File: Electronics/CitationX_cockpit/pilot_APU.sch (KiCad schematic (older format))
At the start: 11 parts

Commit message: Electronics - Working on APUs
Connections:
- net DIO4: now also J?.10 (Pin_10)
- no-connect marks 9 -> 15
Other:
- moved on the sheet: J?
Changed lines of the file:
@@
 EELAYER 26 0
 EELAYER END
-$Descr A3 11693 16535 portrait
+$Descr A4 11693 8268
 encoding utf-8
 Sheet 6 10
@@
 L Connector:Screw_Terminal_01x10 J?
 U 1 1 5DC01A51
-P 7700 1750
+P 8000 1650
 AR Path="/5DB6029E/5DC01A51" Ref="J?"  Part="1"
 AR Path="/5DC174D6/5DC01A51" Ref="J?"  Part="1"
-F 0 "J?" H 7620 1117 50  0000 C CNN
-F 1 "Screw_Terminal_01x10" H 7620 1116 50  0001 C CNN
-F 2 "" H 7700 1750 50  0001 C CNN
-F 3 "~" H 7700 1750 50  0001 C CNN
-	1    7700 1750
-	-1   0    0    1
-$EndComp
-Text Label 7900 2150 0    50   ~ 0
+F 0 "J?" H 7920 1017 50  0000 C CNN
+F 1 "Screw_Terminal_01x10" H 7920 1016 50  0001 C CNN
+F 2 "" H 8000 1650 50  0001 C CNN
+F 3 "~" H 8000 1650 50  0001 C CNN
+	1    8000 1650
+	1    0    0    -1
+$EndComp
+Text Label 7800 1250 2    50   ~ 0
 CLK0
-Text Label 7900 2050 0    50   ~ 0
+Text Label 7800 1350 2    50   ~ 0
 DIO0
-Text Label 7900 1950 0    50   ~ 0
+Text Label 7800 1450 2    50   ~ 0
 CLK1
-Text Label 7900 1850 0    50   ~ 0
+Text Label 7800 1550 2    50   ~ 0
 DIO1
-Text Label 7900 1750 0    50   ~ 0
+Text Label 7800 1650 2    50   ~ 0
 CLK2
-Text Label 7900 1650 0    50   ~ 0
+Text Label 7800 1750 2    50   ~ 0
 DIO2
-Text Label 7900 1550 0    50   ~ 0
+Text Label 7800 1850 2    50   ~ 0
 CLK3
-Text Label 7900 1450 0    50   ~ 0
+Text Label 7800 1950 2    50   ~ 0
 DIO3
-Text Label 7900 1350 0    50   ~ 0
+Text Label 7800 2050 2    50   ~ 0
 CLK4
 $Comp
 L Connector:Screw_Terminal_01x10 J?
 U 1 1 5DC01A64
-P 8300 1750
+P 8700 1650
 AR Path="/5DB6029E/5DC01A64" Ref="J?"  Part="1"
 AR Path="/5DC174D6/5DC01A64" Ref="J?"  Part="1"
-F 0 "J?" H 8220 1117 50  0000 C CNN
-F 1 "Screw_Terminal_01x10" H 8220 1116 50  0001 C CNN
-F 2 "" H 8300 1750 50  0001 C CNN
-F 3 "~" H 8300 1750 50  0001 C CNN
-	1    8300 1750
-	-1   0    0    1
+F 0 "J?" H 8620 1017 50  0000 C CNN
+F 1 "Screw_Terminal_01x10" H 8620 1016 50  0001 C CNN
+F 2 "" H 8700 1650 50  0001 C CNN
+F 3 "~" H 8700 1650 50  0001 C CNN
+	1    8700 1650
+	1    0    0    -1
 $EndComp
 $Comp
 L power:+5V #PWR?
 U 1 1 5DC01A78
-P 8500 1550
+P 8500 1850
 AR Path="/5DB6029E/5DC01A78" Ref="#PWR?"  Part="1"
 AR Path="/5DC174D6/5DC01A78" Ref="#PWR?"  Part="1"
-F 0 "#PWR?" H 8500 1400 50  0001 C CNN
-F 1 "+5V" V 8515 1678 50  0000 L CNN
+F 0 "#PWR?" H 8500 1700 50  0001 C CNN
+F 1 "+5V" V 8515 1978 50  0000 L CNN
+F 2 "" H 8500 1850 50  0001 C CNN
+F 3 "" H 8500 1850 50  0001 C CNN
+	1    8500 1850
+	0    -1   -1   0
+$EndComp
+$Comp
+L power:+5V #PWR?
+U 1 1 5DC01A7E
+P 8500 1950
+AR Path="/5DB6029E/5DC01A7E" Ref="#PWR?"  Part="1"
+AR Path="/5DC174D6/5DC01A7E" Ref="#PWR?"  Part="1"
+F 0 "#PWR?" H 8500 1800 50  0001 C CNN
+F 1 "+5V" V 8515 2078 50  0000 L CNN
+F 2 "" H 8500 1950 50  0001 C CNN
+F 3 "" H 8500 1950 50  0001 C CNN
+	1    8500 1950
+	0    -1   -1   0
+$EndComp
+$Comp
+L power:+5V #PWR?
+U 1 1 5DC01A84
+P 8500 2050
+AR Path="/5DB6029E/5DC01A84" Ref="#PWR?"  Part="1"
+AR Path="/5DC174D6/5DC01A84" Ref="#PWR?"  Part="1"
+F 0 "#PWR?" H 8500 1900 50  0001 C CNN
+F 1 "+5V" V 8515 2178 50  0000 L CNN
+F 2 "" H 8500 2050 50  0001 C CNN
+F 3 "" H 8500 2050 50  0001 C CNN
+	1    8500 2050
+	0    -1   -1   0
+$EndComp
+$Comp
+L power:+5V #PWR?
+U 1 1 5DC01A8A
+P 8500 2150
+AR Path="/5DB6029E/5DC01A8A" Ref="#PWR?"  Part="1"
+AR Path="/5DC174D6/5DC01A8A" Ref="#PWR?"  Part="1"
+F 0 "#PWR?" H 8500 2000 50  0001 C CNN
+F 1 "+5V" V 8515 2278 50  0000 L CNN
+F 2 "" H 8500 2150 50  0001 C CNN
+F 3 "" H 8500 2150 50  0001 C CNN
+	1    8500 2150
+	0    -1   -1   0
+$EndComp
+$Comp
+L power:GND #PWR?
+U 1 1 5DC01AA2
+P 8500 1250
+AR Path="/5DB6029E/5DC01AA2" Ref="#PWR?"  Part="1"
+AR Path="/5DC174D6/5DC01AA2" Ref="#PWR?"  Part="1"
+F 0 "#PWR?" H 8500 1000 50  0001 C CNN
+F 1 "GND" H 8505 1077 50  0000 C CNN
+F 2 "" H 8500 1250 50  0001 C CNN
+F 3 "" H 8500 1250 50  0001 C CNN
+	1    8500 1250
+	0    1    1    0
+$EndComp
+$Comp
+L power:GND #PWR?
+U 1 1 5DC01AA8
+P 8500 1350
+AR Path="/5DB6029E/5DC01AA8" Ref="#PWR?"  Part="1"
+AR Path="/5DC174D6/5DC01AA8" Ref="#PWR?"  Part="1"
+F 0 "#PWR?" H 8500 1100 50  0001 C CNN
+F 1 "GND" H 8505 1177 50  0000 C CNN
+F 2 "" H 8500 1350 50  0001 C CNN
+F 3 "" H 8500 1350 50  0001 C CNN
+	1    8500 1350
+	0    1    1    0
+$EndComp
+$Comp
+L power:GND #PWR?
+U 1 1 5DC01AAE
+P 8500 1450
+AR Path="/5DB6029E/5DC01AAE" Ref="#PWR?"  Part="1"
+AR Path="/5DC174D6/5DC01AAE" Ref="#PWR?"  Part="1"
+F 0 "#PWR?" H 8500 1200 50  0001 C CNN
+F 1 "GND" H 8505 1277 50  0000 C CNN
+F 2 "" H 8500 1450 50  0001 C CNN
+F 3 "" H 8500 1450 50  0001 C CNN
+	1    8500 1450
+	0    1    1    0
+$EndComp
+$Comp
+L power:GND #PWR?
+U 1 1 5DC01AB4
+P 8500 1550
+AR Path="/5DB6029E/5DC01AB4" Ref="#PWR?"  Part="1"
+AR Path="/5DC174D6/5DC01AB4" Ref="#PWR?"  Part="1"
+F 0 "#PWR?" H 8500 1300 50  0001 C CNN
+F 1 "GND" H 8505 1377 50  0000 C CNN
 F 2 "" H 8500 1550 50  0001 C CNN
 F 3 "" H 8500 1550 50  0001 C CNN
@@
 $EndComp
 $Comp
-L power:+5V #PWR?
-U 1 1 5DC01A7E
-P 8500 1450
-AR Path="/5DB6029E/5DC01A7E" Ref="#PWR?"  Part="1"
-AR Path="/5DC174D6/5DC01A7E" Ref="#PWR?"  Part="1"
-F 0 "#PWR?" H 8500 1300 50  0001 C CNN
-F 1 "+5V" V 8515 1578 50  0000 L CNN
-F 2 "" H 8500 1450 50  0001 C CNN
-F 3 "" H 8500 1450 50  0001 C CNN
-	1    8500 1450
-	0    1    1    0
-$EndComp
-$Comp
-L power:+5V #PWR?
-U 1 1 5DC01A84
-P 8500 1350
-AR Path="/5DB6029E/5DC01A84" Ref="#PWR?"  Part="1"
-AR Path="/5DC174D6/5DC01A84" Ref="#PWR?"  Part="1"
-F 0 "#PWR?" H 8500 1200 50  0001 C CNN
-F 1 "+5V" V 8515 1478 50  0000 L CNN
-F 2 "" H 8500 1350 50  0001 C CNN
-F 3 "" H 8500 1350 50  0001 C CNN
-	1    8500 1350
-	0    1    1    0
-$EndComp
-$Comp
-L power:+5V #PWR?
-U 1 1 5DC01A8A
-P 8500 1250
-AR Path="/5DB6029E/5DC01A8A" Ref="#PWR?"  Part="1"
-AR Path="/5DC174D6/5DC01A8A" Ref="#PWR?"  Part="1"
-F 0 "#PWR?" H 8500 1100 50  0001 C CNN
-F 1 "+5V" V 8515 1378 50  0000 L CNN
-F 2 "" H 8500 1250 50  0001 C CNN
-F 3 "" H 8500 1250 50  0001 C CNN
-	1    8500 1250
-	0    1    1    0
-$EndComp
-$Comp
-L power:GND #PWR?
-U 1 1 5DC01AA2
-P 8500 2150
-AR Path="/5DB6029E/5DC01AA2" Ref="#PWR?"  Part="1"
-AR Path="/5DC174D6/5DC01AA2" Ref="#PWR?"  Part="1"
-F 0 "#PWR?" H 8500 1900 50  0001 C CNN
-F 1 "GND" H 8505 1977 50  0000 C CNN
-F 2 "" H 8500 2150 50  0001 C CNN
-F 3 "" H 8500 2150 50  0001 C CNN
-	1    8500 2150
-	0    -1   -1   0
-$EndComp
-$Comp
-L power:GND #PWR?
-U 1 1 5DC01AA8
-P 8500 2050
-AR Path="/5DB6029E/5DC01AA8" Ref="#PWR?"  Part="1"
-AR Path="/5DC174D6/5DC01AA8" Ref="#PWR?"  Part="1"
-F 0 "#PWR?" H 8500 1800 50  0001 C CNN
-F 1 "GND" H 8505 1877 50  0000 C CNN
-F 2 "" H 8500 2050 50  0001 C CNN
-F 3 "" H 8500 2050 50  0001 C CNN
-	1    8500 2050
-	0    -1   -1   0
-$EndComp
-$Comp
-L power:GND #PWR?
-U 1 1 5DC01AAE
-P 8500 1950
-AR Path="/5DB6029E/5DC01AAE" Ref="#PWR?"  Part="1"
-AR Path="/5DC174D6/5DC01AAE" Ref="#PWR?"  Part="1"
-F 0 "#PWR?" H 8500 1700 50  0001 C CNN
-F 1 "GND" H 8505 1777 50  0000 C CNN
-F 2 "" H 8500 1950 50  0001 C CNN
-F 3 "" H 8500 1950 50  0001 C CNN
-	1    8500 1950
-	0    -1   -1   0
-$EndComp
-$Comp
-L power:GND #PWR?
-U 1 1 5DC01AB4
-P 8500 1850
-AR Path="/5DB6029E/5DC01AB4" Ref="#PWR?"  Part="1"
-AR Path="/5DC174D6/5DC01AB4" Ref="#PWR?"  Part="1"
-F 0 "#PWR?" H 8500 1600 50  0001 C CNN
-F 1 "GND" H 8505 1677 50  0000 C CNN
-F 2 "" H 8500 1850 50  0001 C CNN
-F 3 "" H 8500 1850 50  0001 C CNN
-	1    8500 1850
-	0    -1   -1   0
-$EndComp
-$Comp
 L power:GND #PWR?
 U 1 1 5DC01ABA
-P 8500 1750
+P 8500 1650
 AR Path="/5DB6029E/5DC01ABA" Ref="#PWR?"  Part="1"
 AR Path="/5DC174D6/5DC01ABA" Ref="#PWR?"  Part="1"
-F 0 "#PWR?" H 8500 1500 50  0001 C CNN
-F 1 "GND" H 8505 1577 50  0000 C CNN
-F 2 "" H 8500 1750 50  0001 C CNN
-F 3 "" H 8500 1750 50  0001 C CNN
-	1    8500 1750
-	0    -1   -1   0
+F 0 "#PWR?" H 8500 1400 50  0001 C CNN
+F 1 "GND" H 8505 1477 50  0000 C CNN
+F 2 "" H 8500 1650 50  0001 C CNN
+F 3 "" H 8500 1650 50  0001 C CNN
+	1    8500 1650
+	0    1    1    0
 $EndComp
 Wire Notes Line
@@
 L power:+5V #PWR?
 U 1 1 5DC01BE0
-P 8450 1650
+P 8550 1750
 AR Path="/5DB6029E/5DC01BE0" Ref="#PWR?"  Part="1"
 AR Path="/5DC174D6/5DC01BE0" Ref="#PWR?"  Part="1"
-F 0 "#PWR?" H 8450 1500 50  0001 C CNN
-F 1 "+5V" V 8465 1778 50  0000 L CNN
-F 2 "" H 8450 1650 50  0001 C CNN
-F 3 "" H 8450 1650 50  0001 C CNN
-	1    8450 1650
-	0    1    1    0
+F 0 "#PWR?" H 8550 1600 50  0001 C CNN
+F 1 "+5V" V 8565 1878 50  0000 L CNN
+F 2 "" H 8550 1750 50  0001 C CNN
+F 3 "" H 8550 1750 50  0001 C CNN
+	1    8550 1750
+	0    -1   -1   0
 $EndComp
 $Comp
@@
 Wire Wire Line
 	4750 3950 5450 3950
+Text Label 7800 2150 2    50   ~ 0
+DIO4
+NoConn ~ 6600 1850
+NoConn ~ 6600 1950
+NoConn ~ 6600 2050
+NoConn ~ 5100 1850
+NoConn ~ 5100 1950
+NoConn ~ 5100 2050
 $EndSCHEMATC

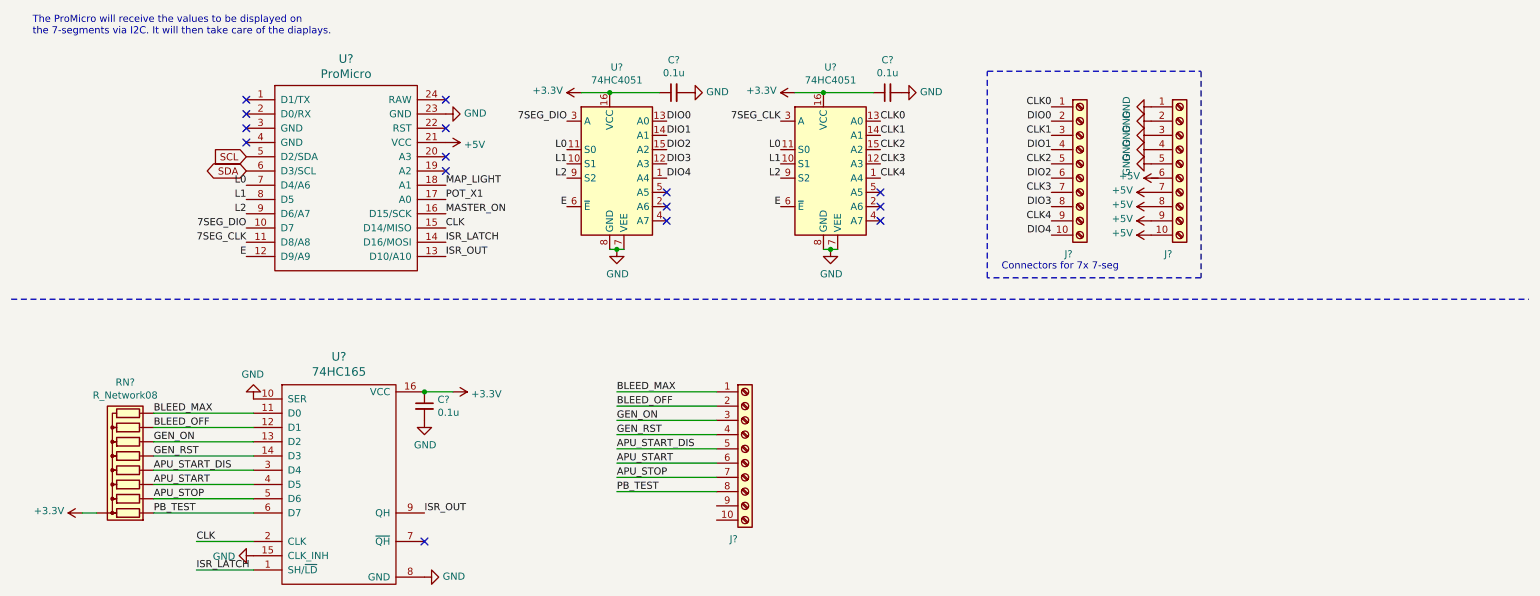
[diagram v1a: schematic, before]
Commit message: Electronics - Misc. works
Continued (and checked board). All connections are probably OK.
Fixed hierarchical pins in APUs (affects all schematics)
Numbered elements for testing schematics
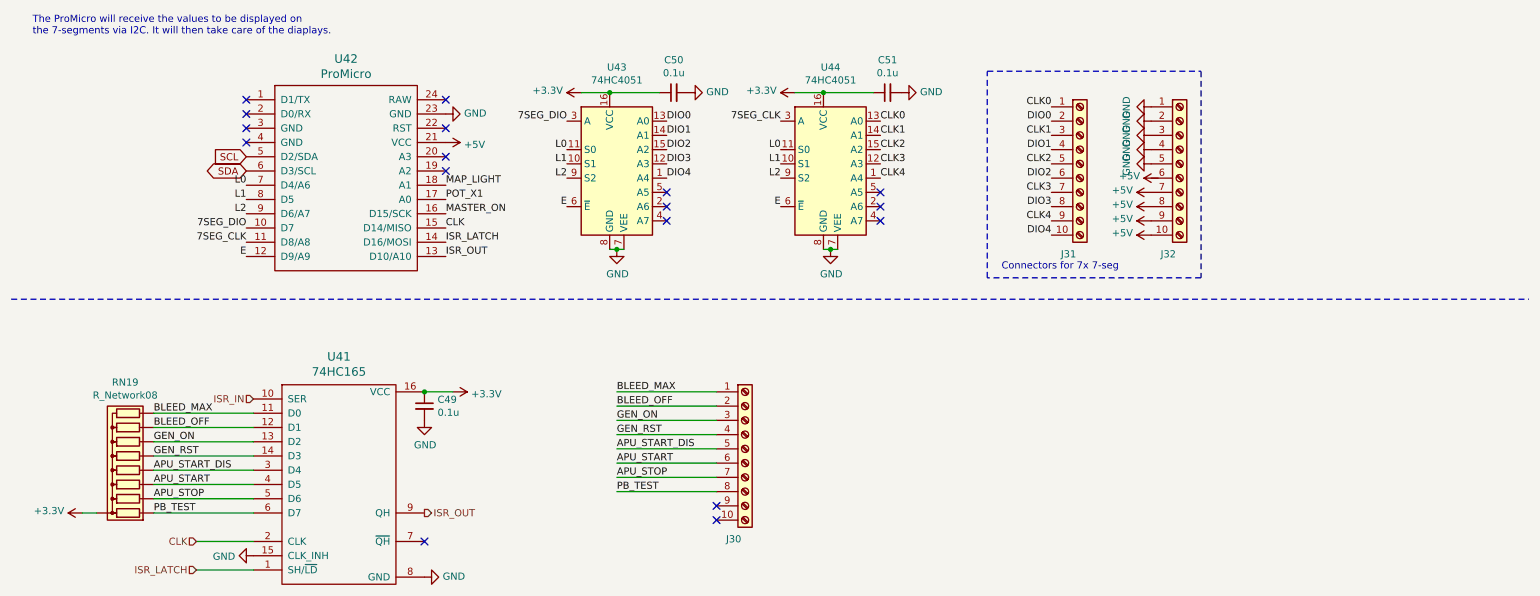
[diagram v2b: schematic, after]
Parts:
- gave numbers to parts that had none: 11
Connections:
- net GND: no longer U41.10 (SER)
- new net ISR_IN: U41.10 (SER)
- no-connect marks 15 -> 17

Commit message: Electronics - APU pilot UART and bibbon cable
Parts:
- added J?: Conn_02x08_Odd_Even, symbol Connector_Generic:Conn_02x08_Odd_Even
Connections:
- net labels added: RST, RX, TX
- net labels removed: ISR_IN
- wire segments 28 -> 26
- no-connect marks 17 -> 14
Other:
- note added: "Connectors for 7x 7-seg and OLED\n"
- note added: "RST can be used to restart the Pro Micro.\nThis pin is pulled high by a 10k resistor on the board, \nand is active-low, so it must be connected to ground to initiate a reset.\nThe Pro Micro will remain "off" until the reset line is pulled back to high."
- note added: "SCL and SDA are used for an OLED\n"
- note added: "This board will be separated from the rest.\nIw ill communicate with the master using USART (TTL level, no need for MAX232)"
- note removed: "Connectors for 7x 7-seg"
- note removed: "The ProMicro will receive the values to be displayed on \nthe 7-segments via I2C. It will then take care of the diaplays."
